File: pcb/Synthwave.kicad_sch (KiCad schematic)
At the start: 61 parts, among them J1 Barrel_Jack_Switch, J11 ELEC1 FLOAT1, J12 Conn_01x04_Socket, J2 Conn_01x06_Socket, J3 SDA, J4 Conn_01x06_Socket, J5 ADC3, J6 ADC4, J7 Conn_01x04_Socket, J8 Conn_01x04_Socket, Q1 TIP120, Q10 TIP120, Q2 TIP120, Q3 TIP120, Q4 TIP120, Q5 TIP120, Q6 TIP120, Q7 TIP120, Q8 TIP120, Q9 TIP120, U1 Heltec_HTIT-WB32v3, U2 L9110, U3 L7805, U4 XL4015-5A-PS

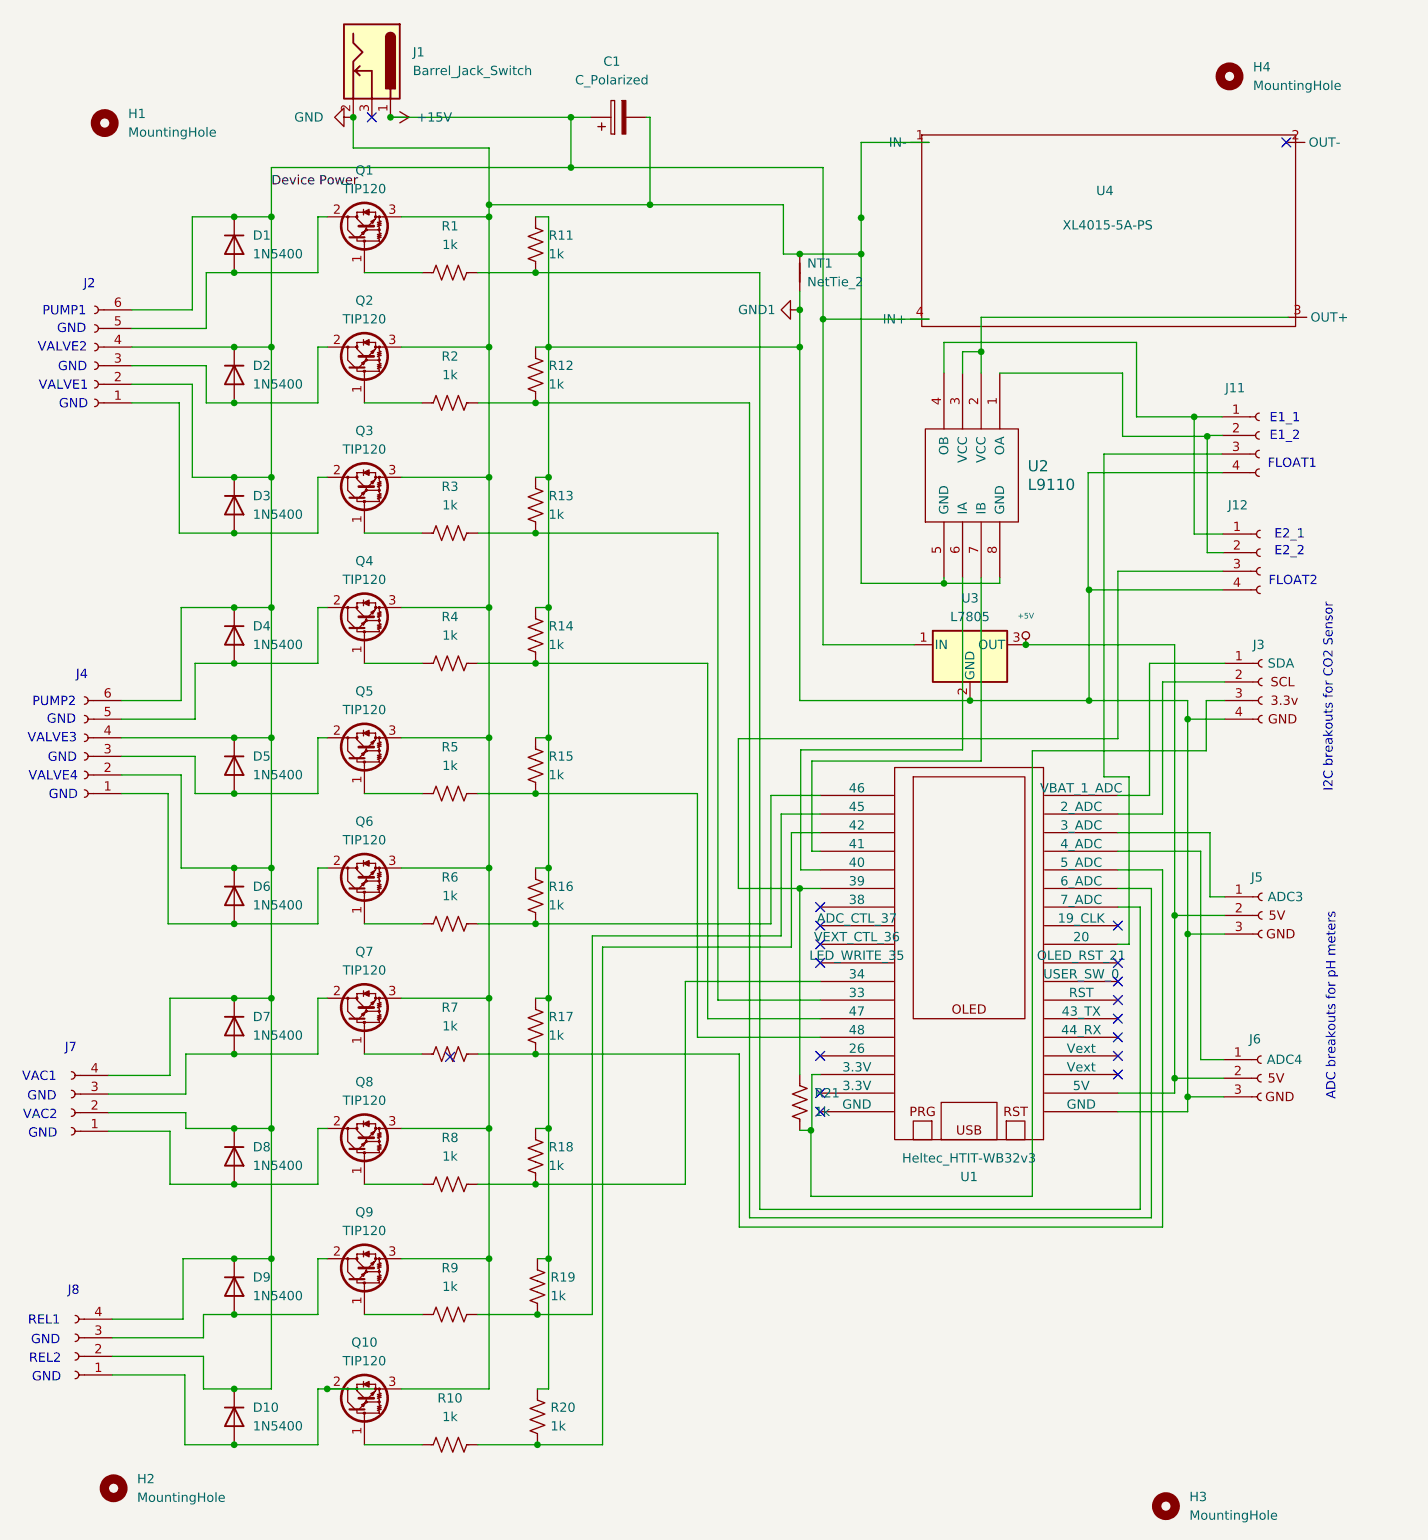
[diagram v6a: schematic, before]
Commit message: Finish autorouting.  Updates to electrode holder and container cover
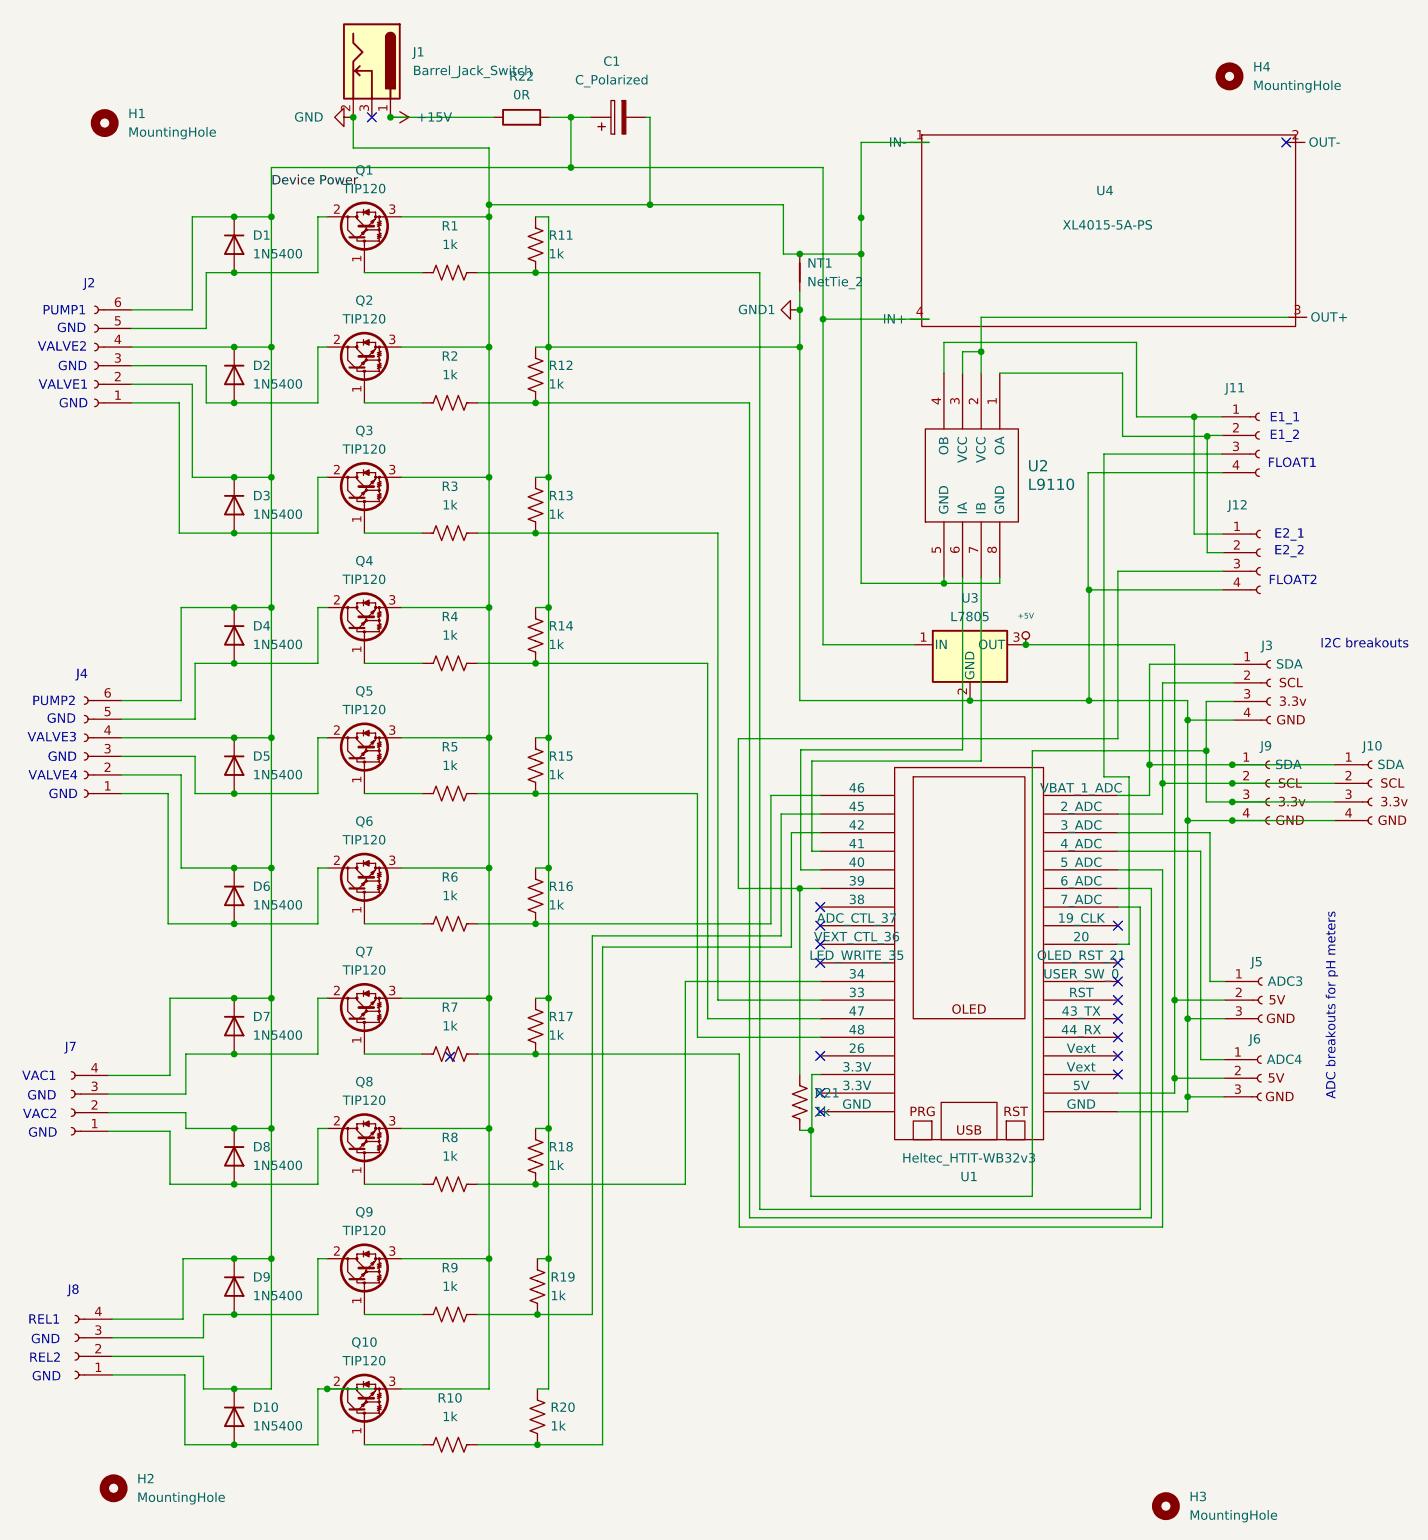
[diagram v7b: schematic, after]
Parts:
- added J10, J9: SDA, Connector_JST:JST_XH_S4B-XH-A_1x04_P2.50mm_Horizontal, symbol Connector:Conn_01x04_Socket
- added R22: 0R, Connector_PinHeader_2.54mm:PinHeader_1x02_P2.54mm_Vertical, symbol Device:R
- C1: footprint Capacitor_THT:CP_Radial_D10.0mm_P7.50mm -> Capacitor_THT:CP_Radial_D7.5mm_P2.50mm
- J5, J6: footprint Connector_JST:JST_PH_S3B-PH-K_1x03_P2.00mm_Horizontal -> Connector_PinHeader_2.54mm:PinHeader_1x03_P2.54mm_Vertical
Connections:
- net +15V: now also R22.1; no longer C1.1, D1.1 (K), D10.1 (K), D2.1 (K), D3.1 (K), D4.1 (K), D5.1 (K), D6.1 (K), D7.1 (K), D8.1 (K), D9.1 (K), J2.2 (Pin_2), J2.4 (Pin_4), J2.6 (Pin_6), J4.2 (Pin_2), J4.4 (Pin_4), J4.6 (Pin_6), J7.2 (Pin_2), J7.4 (Pin_4), J8.2 (Pin_2), J8.4 (Pin_4), U3.1 (IN), U4.4 (IN+)
- net GND1: now also J10.4 (Pin_4), J9.4 (Pin_4)
- net at J3.1 (Pin_1), U1.36 (VBAT_1_ADC): now also J10.1 (Pin_1), J9.1 (Pin_1)
- net at J3.2 (Pin_2), U1.37 (2_ADC): now also J10.2 (Pin_2), J9.2 (Pin_2)
- net at J3.3 (Pin_3), R21.1, U1.11 (3.3V): now also J10.3 (Pin_3), J9.3 (Pin_3)
- new net Device Power: C1.1, D1.1 (K), D10.1 (K), D2.1 (K), D3.1 (K), D4.1 (K), D5.1 (K), D6.1 (K), D7.1 (K), D8.1 (K), D9.1 (K), J2.2 (Pin_2), J2.4 (Pin_4), J2.6 (Pin_6), J4.2 (Pin_2), J4.4 (Pin_4), J4.6 (Pin_6), J7.2 (Pin_2), J7.4 (Pin_4), J8.2 (Pin_2), J8.4 (Pin_4), R22.2, U3.1 (IN), U4.4 (IN+)
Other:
- note added: "I2C breakouts"
- note removed: "I2C breakouts for CO2 Sensor"
- moved on the sheet: J3, J5
